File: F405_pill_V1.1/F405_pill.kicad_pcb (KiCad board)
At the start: 4 copper layers, 53.8 x 19.4 mm, 50 parts, among them J1 Conn_01x04_Male, J2 Conn_01x04_Male, J4 TYPE-C-31-M-12, U1 STM32F405RGTx, U2 MAX3051EKA+T, U3 LM1117-3.3, U4 STM32F405_pill, U5 HT7550-1, Y1 Crystal_GND24

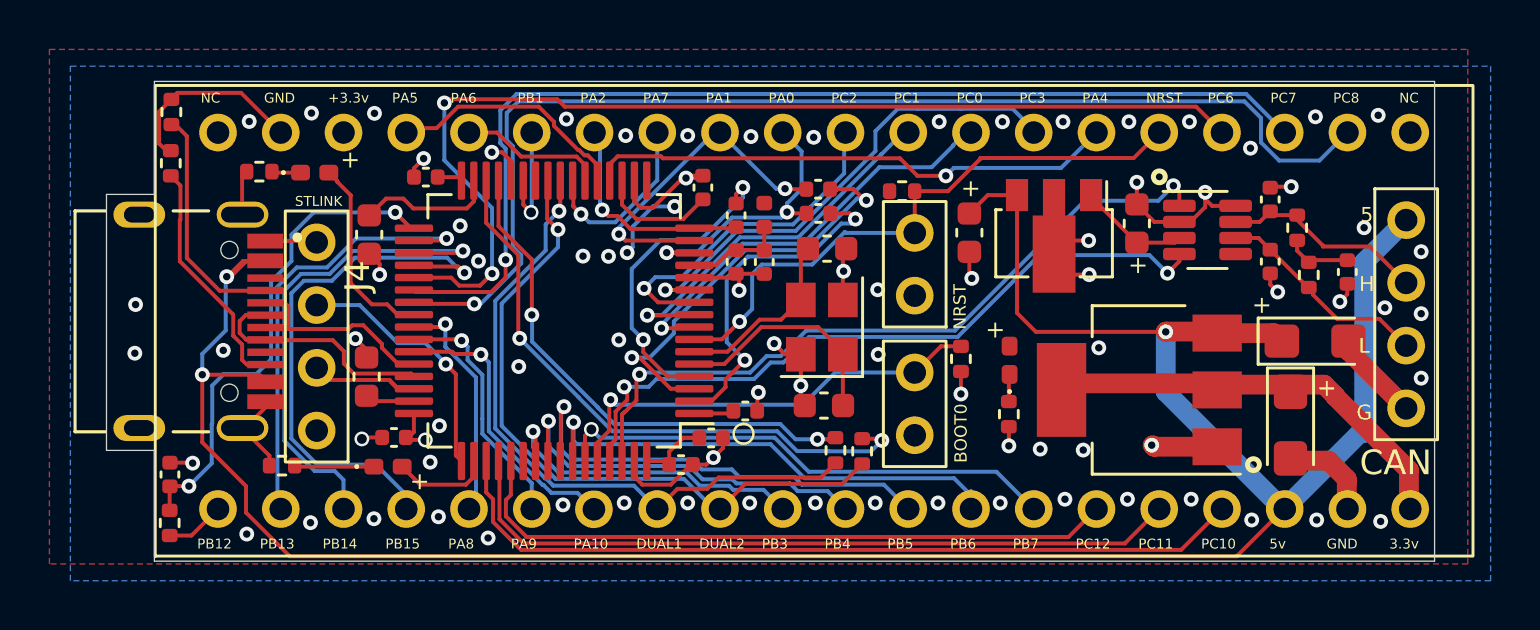
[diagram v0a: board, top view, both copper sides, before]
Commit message: added a lot of LCSC#s
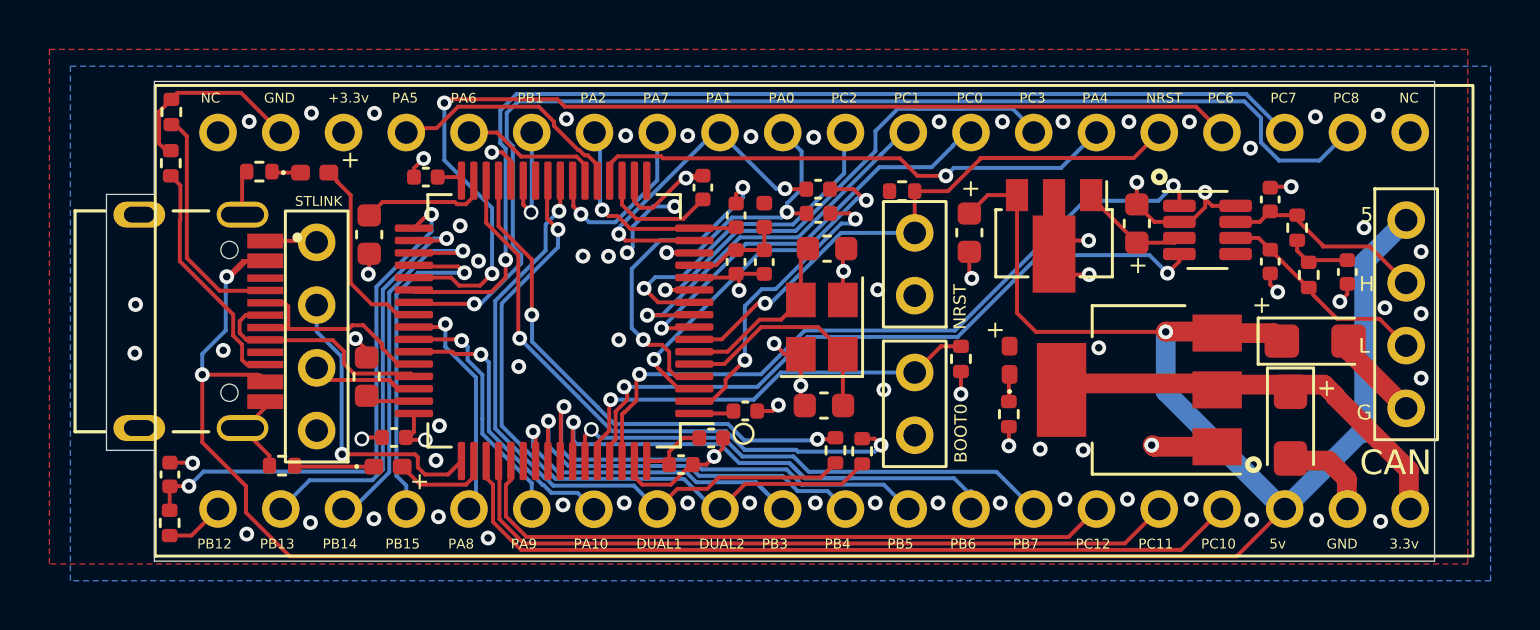
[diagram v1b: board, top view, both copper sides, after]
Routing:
- net PB15: track 22.1 -> 14.1 mm
- net PB14: track 20.2 -> 15.4 mm
- net PB11: track 24.5 -> 28.6 mm
- net PB6: track 19.9 -> 22.8 mm
- net PC14: track 17.2 -> 15.3 mm
- net PB12: track 20.0 -> 21.8 mm
- net PC13: track 13.9 -> 12.2 mm
- net SWCLK: track 10.4 -> 12.1 mm
- net PB3: track 13.0 -> 14.4 mm
- net PB13: track 18.1 -> 16.9 mm
- net NRST: track 23.4 -> 22.9 mm

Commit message: fixed some LC parts
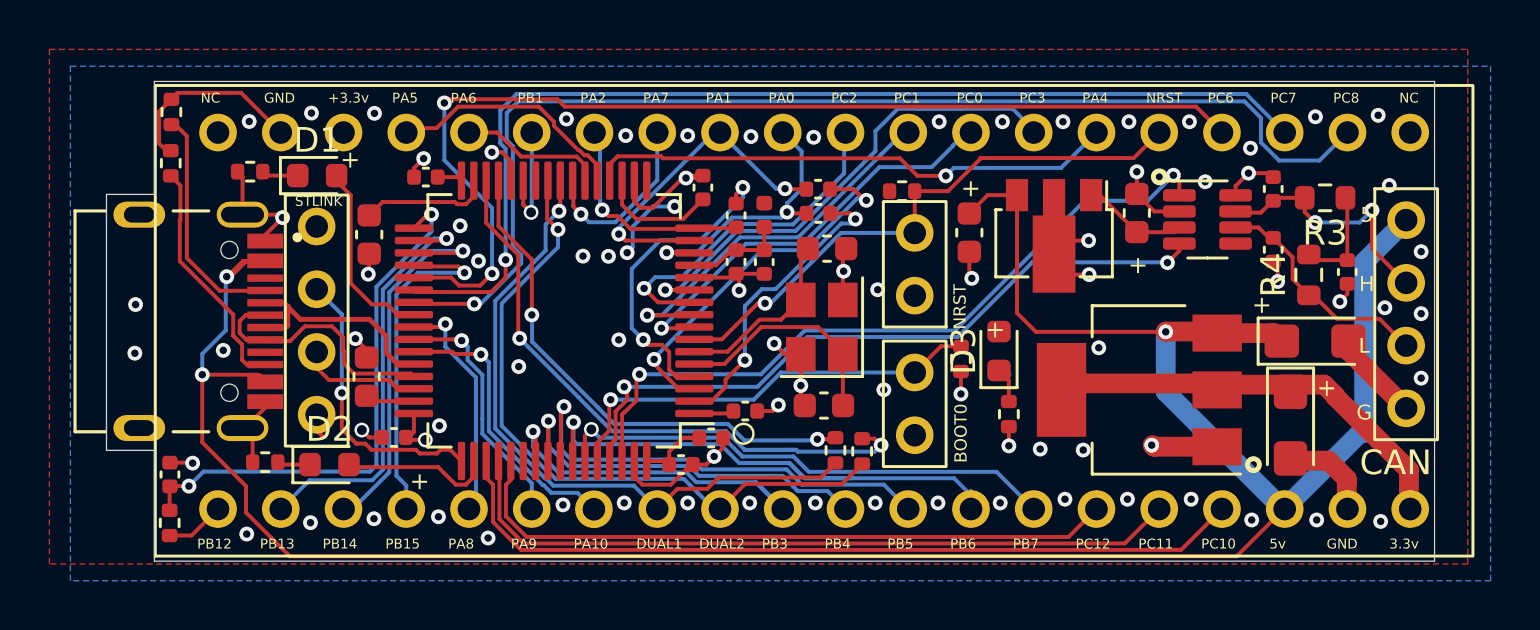
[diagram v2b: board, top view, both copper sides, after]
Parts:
- D1, D2, D3: footprint LED_SMD:LED_0402_1005Metric_Pad0.77x0.64mm_HandSolder -> LED_SMD:LED_0603_1608Metric
- R3, R4: footprint Resistor_SMD:R_0402_1005Metric -> Resistor_SMD:R_0603_1608Metric
- R6: value 47 ohm -> 47R
- moved D2 2.37 mm to (103.4, 90.5)
- moved R3 1.66 mm to (143.7, 79.7), turned to 180 degrees
- moved R5 0.69 mm to (100.8, 90.4)
- moved J2 0.64 mm to (102.9, 84.7)
- moved D3 0.57 mm to (130.5, 85.9)
- moved C15 0.49 mm to (141.6, 81.8)
- moved C14 0.44 mm to (141.6, 79.3)
- moved C22 0.42 mm to (136.1, 80.3)
- moved U2 0.42 mm to (138.9, 80.6)
- moved R7 0.37 mm to (100.2, 78.6)
- moved D1 0.16 mm to (102.9, 78.8)
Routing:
- net PA15: track 3.97 -> 6.16 mm
- net Net-(C14-Pad1): track 8.41 -> 10.6 mm, vias 0 -> 2
- net Net-(D2-Pad1): track 3.22 -> 1.34 mm
- net Net-(C13-Pad1): track 2.31 -> 3.78 mm
- net GND: track 71.2 -> 70.1 mm
- net USB_D+: track 9.72 -> 10.5 mm
- net SWCLK: track 12.1 -> 11.6 mm

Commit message: fiddled with vias
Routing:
- net +3V3: track 33.4 -> 30.2 mm
- net PB6: track 22.8 -> 20.9 mm
- net GND: track 70.1 -> 71.6 mm, vias 73 -> 92
- net +5V: track 101.9 -> 101.2 mm

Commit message: minor edits
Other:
- board size 53.8 x 19.4 mm -> 54.1 x 19.4 mm
- board text removed: "5"
- board text removed: "G"
- board text removed: "H"
- board text removed: "L"

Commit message: minor edits
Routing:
- net GND: track 71.6 -> 72.3 mm
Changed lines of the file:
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@@
     )
   )
-  (gr_circle (center 136.99 78.85) (end 137.230832 78.85) (layer "F.SilkS") (width 0.2) (fill none))
+  (gr_circle (center 136.99 78.6) (end 137.230832 78.6) (layer "F.SilkS") (width 0.2) (fill none))
   (gr_circle (center 140.8 90.5) (end 141.040832 90.5) (layer "F.SilkS") (width 0.2) (fill none))
   (gr_circle (center 120.16 89.25) (end 120.56 89.25) (layer "F.SilkS") (width 0.1) (fill none))
@@
   (segment (start 122.48 86.033) (end 122.48 87.949) (width 0.16) (layer "F.Cu") (net 2))
   (segment (start 122.48 86.033) (end 121.833 86.033) (width 0.16) (layer "F.Cu") (net 2))
-  (segment (start 104.901 86.163) (end 104.901 85.851) (width 0.16) (layer "F.Cu") (net 2))
   (segment (start 124.18 82.021) (end 124.443 81.758) (width 0.16) (layer "F.Cu") (net 2))
   (segment (start 100.29 90.4) (end 100.29 89.43) (width 0.16) (layer "F.Cu") (net 2))
@@
   (segment (start 144.6 83.6) (end 144.3 83.9) (width 0.16) (layer "F.Cu") (net 2))
   (segment (start 110.742 78.211) (end 110.38656 77.85556) (width 0.16) (layer "F.Cu") (net 2))
+  (segment (start 104.901 86.163) (end 104.901 85.401) (width 0.16) (layer "F.Cu") (net 2))
   (segment (start 144.579 91.221) (end 144.579 91.079) (width 0.8) (layer "F.Cu") (net 2))
   (segment (start 96.5 77.5) (end 96.79 77.79) (width 0.16) (layer "F.Cu") (net 2))
@@
   (segment (start 132.73 79.6775) (end 132.73 80.85) (width 0.16) (layer "F.Cu") (net 2))
   (segment (start 141.782 82.462) (end 141.6 82.28) (width 0.16) (layer "F.Cu") (net 2))
-  (segment (start 106.82 78.86) (end 106.82 78.5) (width 0.16) (layer "F.Cu") (net 2))
   (segment (start 138.873 89.7756) (end 136.782 89.7756) (width 0.8) (layer "F.Cu") (net 2))
   (segment (start 140.0775 79.2225) (end 140.6 78.7) (width 0.16) (layer "F.Cu") (net 2))
-  (segment (start 104.901 85.851) (end 104.45 85.4) (width 0.16) (layer "F.Cu") (net 2))
   (segment (start 140.6 78.7) (end 141.437 78.7) (width 0.16) (layer "F.Cu") (net 2))
   (segment (start 100.795 81.45) (end 100.795 81.205) (width 0.16) (layer "F.Cu") (net 2))
@@
   (segment (start 116.001315 80.104) (end 116.489253 80.104) (width 0.16) (layer "F.Cu") (net 2))
   (segment (start 119.98 83.45) (end 119.98 82.896) (width 0.16) (layer "F.Cu") (net 2))
+  (segment (start 104.901 85.401) (end 104.8 85.3) (width 0.16) (layer "F.Cu") (net 2))
   (segment (start 118.03 90.5) (end 118.11 90.5) (width 0.16) (layer "F.Cu") (net 2))
   (segment (start 136.08 79.54) (end 136.08 78.645) (width 0.16) (layer "F.Cu") (net 2))
@@
   (segment (start 96.5 76.215) (end 96.5 77.5) (width 0.16) (layer "F.Cu") (net 2))
   (segment (start 116.489253 80.104) (end 117.790253 78.803) (width 0.16) (layer "F.Cu") (net 2))
-  (segment (start 106.82 78.5) (end 107.21 78.11) (width 0.16) (layer "F.Cu") (net 2))
   (segment (start 118.654152 90.5) (end 118.94 90.214152) (width 0.16) (layer "F.Cu") (net 2))
   (segment (start 129.3 81.885) (end 129.3 82.86) (width 0.16) (layer "F.Cu") (net 2))
@@
   (segment (start 121.33 88.33) (end 121.57 88.09) (width 0.16) (layer "F.Cu") (net 2))
   (segment (start 137.8025 80.25) (end 136.79 80.25) (width 0.16) (layer "F.Cu") (net 2))
+  (segment (start 106.82 78.86) (end 106.14 78.86) (width 0.16) (layer "F.Cu") (net 2))
   (segment (start 120.71 88.33) (end 121.33 88.33) (width 0.16) (layer "F.Cu") (net 2))
+  (segment (start 121 82.78) (end 121.42 82.78) (width 0.16) (layer "F.Cu") (net 2))
   (segment (start 146.982 88.222) (end 144.65 85.89) (width 0.8) (layer "F.Cu") (net 2))
+  (segment (start 121.7 82.5) (end 121.7 82.4) (width 0.16) (layer "F.Cu") (net 2))
   (segment (start 136.79 80.25) (end 136.08 79.54) (width 0.16) (layer "F.Cu") (net 2))
   (segment (start 133.31 81.43) (end 134.13 81.43) (width 0.16) (layer "F.Cu") (net 2))
@@
   (segment (start 117.221 91.309) (end 118.03 90.5) (width 0.16) (layer "F.Cu") (net 2))
   (segment (start 136.782 89.7756) (end 136.7184 89.712) (width 0.8) (layer "F.Cu") (net 2))
+  (segment (start 106.14 78.86) (end 106.1 78.9) (width 0.16) (layer "F.Cu") (net 2))
+  (segment (start 121.42 82.78) (end 121.7 82.5) (width 0.16) (layer "F.Cu") (net 2))
   (segment (start 115.742 91.242) (end 115.809 91.309) (width 0.16) (layer "F.Cu") (net 2))
   (segment (start 97 75.715) (end 96.5 76.215) (width 0.16) (layer "F.Cu") (net 2))
@@
   (via (at 138.847972 79.049343) (size 0.6) (drill 0.3) (layers "F.Cu" "B.Cu") (net 2))
   (via (at 123.065943 92.05) (size 0.6) (drill 0.3) (layers "F.Cu" "B.Cu") (free) (net 2))
-  (via (at 121.5 82.6) (size 0.6) (drill 0.3) (layers "F.Cu" "B.Cu") (net 2))
+  (via (at 121.7 82.4) (size 0.6) (drill 0.3) (layers "F.Cu" "B.Cu") (net 2))
   (via (at 105.22 76.28) (size 0.6) (drill 0.3) (layers "F.Cu" "B.Cu") (net 2))
   (via (at 119.98 83.45) (size 0.6) (drill 0.3) (layers "F.Cu" "B.Cu") (net 2))
@@
   (via (at 125.4 80.5) (size 0.6) (drill 0.3) (layers "F.Cu" "B.Cu") (free) (net 2))
   (via (at 123.3 88.3) (size 0.6) (drill 0.3) (layers "F.Cu" "B.Cu") (free) (net 2))
-  (via (at 107.21 78.11) (size 0.6) (drill 0.3) (layers "F.Cu" "B.Cu") (net 2))
+  (via (at 106.1 78.9) (size 0.6) (drill 0.3) (layers "F.Cu" "B.Cu") (net 2))
   (via (at 108.6 87) (size 0.6) (drill 0.3) (layers "F.Cu" "B.Cu") (free) (net 2))
   (via (at 147.59 87) (size 0.6) (drill 0.3) (layers "F.Cu" "B.Cu") (free) (net 2))
@@
   (via (at 130.64 76.62) (size 0.6) (drill 0.3) (layers "F.Cu" "B.Cu") (free) (net 2))
   (via (at 143.36 92.74) (size 0.6) (drill 0.3) (layers "F.Cu" "B.Cu") (free) (net 2))
-  (via (at 104.45 85.4) (size 0.6) (drill 0.3) (layers "F.Cu" "B.Cu") (free) (net 2))
+  (via (at 104.8 85.3) (size 0.6) (drill 0.3) (layers "F.Cu" "B.Cu") (free) (net 2))
   (via (at 125.59 83.42) (size 0.6) (drill 0.3) (layers "F.Cu" "B.Cu") (free) (net 2))
   (via (at 130.55 92.05) (size 0.6) (drill 0.3) (layers "F.Cu" "B.Cu") (free) (net 2))
